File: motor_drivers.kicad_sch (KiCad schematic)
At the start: 20 parts, among them U2 TB6612FNG, U3 TB6612FNG, U9 AMS1117-3.3

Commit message: BOM work
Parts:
- C10: renamed from C41; LCSC (none) -> C29277
- C11: renamed from C1; footprint Capacitor_SMD:CP_Elec_8x10 -> Capacitor_SMD:(EEVTG1E222M); LCSC (none) -> C401984
- C12: renamed from C2; footprint Capacitor_SMD:CP_Elec_8x10 -> Capacitor_SMD:(EEVTG1E222M); LCSC (none) -> C401984
- C9: renamed from C40; LCSC (none) -> C15850
- C_VCC_A1, C_VCC_A2: LCSC (none) -> C17024
- C_VCC_B1, C_VCC_B2, C_VM_B1, C_VM_B2: LCSC (none) -> C1590
- C_VM_A1, C_VM_A2: LCSC (none) -> C15850
- R10: renamed from R1; LCSC (none) -> C25804
- R6: renamed from R7; LCSC (none) -> C25804
- R7: renamed from R8; LCSC (none) -> C25804
- R8: renamed from R9; LCSC (none) -> C25804
- R9: renamed from R10; LCSC (none) -> C25804
- U7: renamed from U9; LCSC (none) -> C6186
- U8: renamed from U2; LCSC (none) -> C88224
- U9: renamed from U3; LCSC (none) -> C88224

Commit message: BOM work
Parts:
- C11, C12: value 2200uF 25V -> 1000uF 25V; footprint Capacitor_SMD:(EEVTG1E222M) -> Capacitor_SMD:CP_Elec_10x10.5; Availability (none) -> In Stock; Check_prices (none) -> https://www.snapeda.com/parts/EEVTG2A221M/Panasonic/view-pa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; Description_1 (none) -> 220µF 100V Aluminum Electrolytic Capacitors Radial, Can - S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; LCSC C401984 -> C7471896; MANUFACTURER (none) -> Panasonic; MAXIMUM_PACKAGE_HEIGHT (none) -> 16.5mm; MF (none) -> Panasonic; MP (none) -> EEVTG2A221M; PARTREV (none) -> 10-Oct-19; Package (none) -> RADIAL-2 Panasonic; Price (none) -> None; STANDARD (none) -> Manufacturer Recommendations; SnapEDA_Link (none) -> https://www.snapeda.com/parts/EEVTG2A221M/Panasonic/view-pa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
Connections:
- net +12V: no longer C9.1
- net +3.3V_MOTOR: no longer C10.1

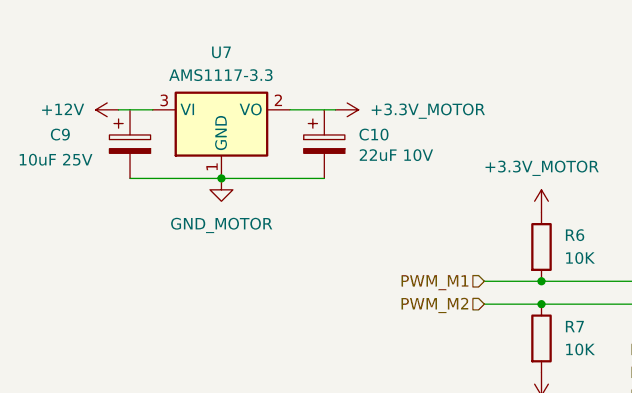
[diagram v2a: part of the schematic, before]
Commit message: Refactored board to use larger vias and route better paths.
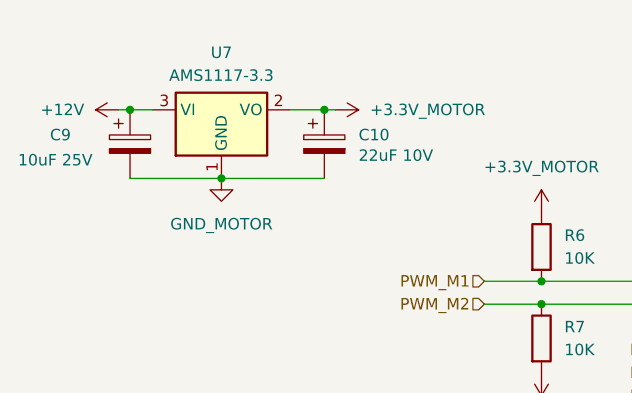
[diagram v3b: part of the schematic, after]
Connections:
- net +12V: now also C9.1
- net +3.3V_MOTOR: now also C10.1
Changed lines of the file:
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@@
+	)
+	(junction
+		(at 45.72 24.13)
+		(diameter 0)
+		(color 0 0 0 0)
 	)
 	(junction
@@
 	)
 	(junction
+		(at 24.13 24.13)
+		(diameter 0)
+		(color 0 0 0 0)
+	)
+	(junction
 		(at 69.85 119.38)
 		(diameter 0)
@@
 	(wire
 		(pts
+			(xy 41.91 24.13) (xy 45.72 24.13)
+		)
+		(stroke
+			(width 0)
+			(type default)
+		)
+	)
+	(wire
+		(pts
 			(xy 34.29 31.75) (xy 45.72 31.75)
 		)
@@
 	(wire
 		(pts
-			(xy 22.86 24.13) (xy 26.67 24.13)
-		)
-		(stroke
-			(width 0)
-			(type default)
-		)
-	)
-	(wire
-		(pts
 			(xy 125.73 25.4) (xy 142.24 25.4)
 		)
@@
 	(wire
 		(pts
-			(xy 41.91 24.13) (xy 46.99 24.13)
-		)
-		(stroke
-			(width 0)
-			(type default)
-		)
-	)
-	(wire
-		(pts
 			(xy 111.76 96.52) (xy 111.76 99.06)
 		)
@@
 	(wire
 		(pts
+			(xy 24.13 24.13) (xy 26.67 24.13)
+		)
+		(stroke
+			(width 0)
+			(type default)
+		)
+	)
+	(wire
+		(pts
 			(xy 137.16 67.31) (xy 146.05 67.31)
 		)
@@
 	(wire
 		(pts
+			(xy 22.86 24.13) (xy 24.13 24.13)
+		)
+		(stroke
+			(width 0)
+			(type default)
+		)
+	)
+	(wire
+		(pts
 			(xy 69.85 43.18) (xy 88.9 43.18)
 		)
@@
 		)
 		(stroke
+			(width 0)
+			(type default)
+		)
+	)
+	(wire
+		(pts
+			(xy 45.72 24.13) (xy 46.99 24.13)
+		)
+		(stroke

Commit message: V 1.2
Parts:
- added D9: Blue, Diode_SMD:D_0805_2012Metric, symbol PCM_JLCPCB-Diodes:LED,0805,Red
- added R_LED3: 1.8K, Resistor_SMD:R_0603_1608Metric, symbol Device:R
- added TP5: STBY, barn_shade_controller:TestPoint_Pad_D1.0mm_No_SolderMask, symbol Connector:TestPoint
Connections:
- net +12V: now also R_LED3.2
- net GND_MOTOR: now also D9.1
- net STBY: now also TP5.1
- new net: D9.2, R_LED3.1
